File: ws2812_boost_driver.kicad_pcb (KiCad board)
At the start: 2 copper layers, 20.5 x 16.5 mm, 24 parts, among them J1 Conn_01x01, J2 Conn_01x01, J3 Conn_01x01, J4 Conn_01x01, J5 Conn_01x01, J6 Conn_01x01, J7 Conn_01x01, J8 Conn_ARM_JTAG_SWD_10, U1 ATSAMD21E15L-A, U2 TC2014-3.3VxCTTR, U3 MCP1640CH, U4 ATtiny10-TS

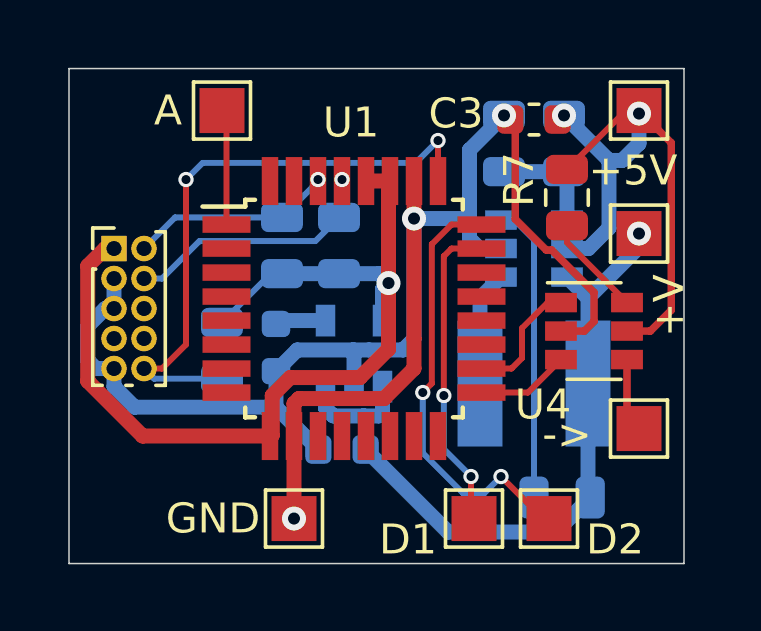
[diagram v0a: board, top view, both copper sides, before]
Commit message: Fix core vreg issue
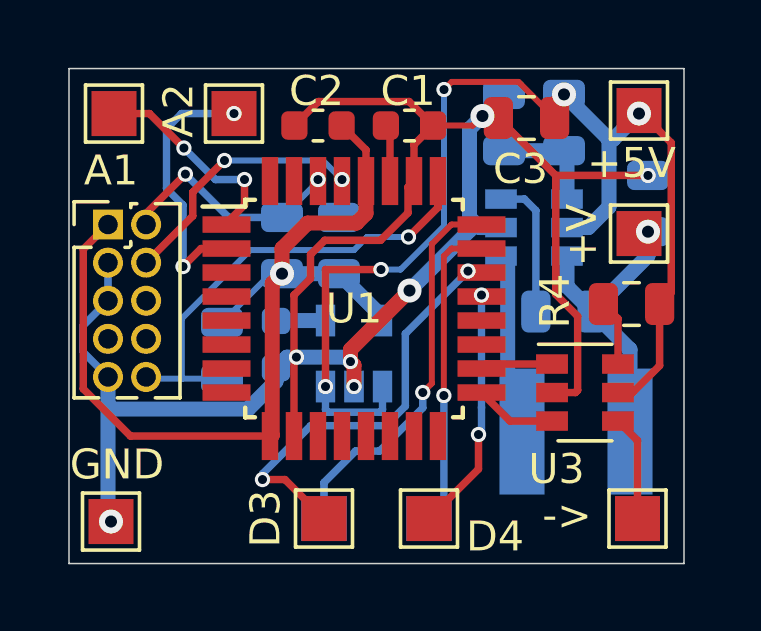
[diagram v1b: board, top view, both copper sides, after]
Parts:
- added C2: 10kpF, Capacitor_SMD:C_0603_1608Metric, F.Cu at (138.3, 88.9)
- added C4: 10kpF, Capacitor_SMD:C_0603_1608Metric, B.Cu at (136.9, 96.2)
- added J10: Conn_01x01, TestPoint:TestPoint_Pad_1.5x1.5mm, F.Cu at (135.5, 88.5)
- added J7: Conn_01x01, TestPoint:TestPoint_Pad_1.5x1.5mm, F.Cu at (138.5, 102.0)
- added J8: Conn_01x01, TestPoint:TestPoint_Pad_1.5x1.5mm, F.Cu at (142.0, 102.0)
- C1: value 0.01uF -> 10kpF; moved to F.Cu
- C3: footprint Capacitor_SMD:C_0603_1608Metric -> Capacitor_SMD:C_0805_2012Metric
- C5: renamed from C2; footprint Capacitor_SMD:C_0603_1608Metric -> Capacitor_SMD:C_0805_2012Metric
- J11: renamed from J8; footprint Connector_PinHeader_1.00mm:PinHeader_2x05_P1.00mm_Vertical -> Connector_PinHeader_1.27mm:PinHeader_2x05_P1.27mm_Vertical
- J5, J6: moved to B.Cu
- moved C5 13.1 mm to (149.3, 91.5), turned to 90 degrees
- moved C1 8.63 mm to (141.3, 88.9), turned to 180 degrees
- moved J5 7.50 mm to (138.5, 102.0)
- moved R5 6.20 mm to (146.5, 95.1)
- moved J4 6.10 mm to (131.4, 102.1)
- moved R4 4.15 mm to (148.8, 94.8), turned to 180 degrees
- moved J9 3.60 mm to (131.5, 88.5)
- moved J3 3.00 mm to (148.9, 102.0)
- moved L1 2.13 mm to (146.9, 99.1)
- moved U3 2.07 mm to (147.2, 97.8)
- moved J6 1.50 mm to (142.0, 102.0)
- moved REF** 1.36 mm to (133.7, 100.8), turned to 90 degrees
- moved J11 0.82 mm to (131.3, 92.2)
- moved R6 0.70 mm to (146.5, 88.8)
- moved R7 0.70 mm to (144.5, 88.8)
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- renumbered J7 to J9, R7 to R4, R4 to R5, R5 to R6, R6 to R7, U4 to U3, U3 to U4
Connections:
- C1 pad 1: Net-(C1-Pad1) -> GND
- C1 pad 2: GND -> Net-(C1-Pad2)
- C5 pad 1: +V -> +2-3V
- J1 pad 1: +V -> +2-3V
- L1 pad 1: +V -> +2-3V
- R5 pad 1: +V -> +2-3V
- U1 pad 2: (no net) -> A2
- U1 pad 21: (no net) -> D4
- U1 pad 22: (no net) -> D3
- U1 pad 27: +3.3V -> Net-(C1-Pad2)
- U2 pad 1: +V -> +5V
- U2 pad 3: +V -> +5V
- U2 pad 4: Net-(C1-Pad1) -> Net-(C4-Pad1)
- U4 pad 6: +V -> +2-3V
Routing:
- net +V: track 24.4 -> 0.00 mm, vias 1 -> 0
- net +5V: track 20.3 -> 40.6 mm, vias 2 -> 5
- net D3: track 0.00 -> 13.8 mm, vias 0 -> 2
- net GND: track 55.7 -> 66.7 mm, vias 3 -> 7
- net +2-3V: track 0.00 -> 10.2 mm, vias 0 -> 1
- net A2: track 0.00 -> 8.98 mm, vias 0 -> 2
- net D4: track 0.00 -> 8.17 mm, vias 0 -> 2
- net Net-(R5-Pad2): track 9.97 -> 4.69 mm
- net RESET: track 20.3 -> 15.5 mm, vias 2 -> 1
- net A1: track 3.86 -> 7.01 mm, vias 0 -> 2
- net Net-(L1-Pad2): track 3.84 -> 6.14 mm
- net Net-(C1-Pad2): track 0.00 -> 1.91 mm
- net SCK: track 4.14 -> 2.41 mm
- net Net-(C4-Pad1): track 0.00 -> 1.70 mm
- net Net-(C1-Pad1): track 1.70 -> 0.00 mm
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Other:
- board text added: "12/06/20"
- board text added: "A1"
- board text added: "A2"
- board text added: "D3"
- board text added: "D4"
- board text added: "v0.0.2"
- board text removed: "11/13/20"
- board text removed: "A"
- board text removed: "v0.0.0"
